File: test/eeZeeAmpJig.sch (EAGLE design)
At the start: 19 parts

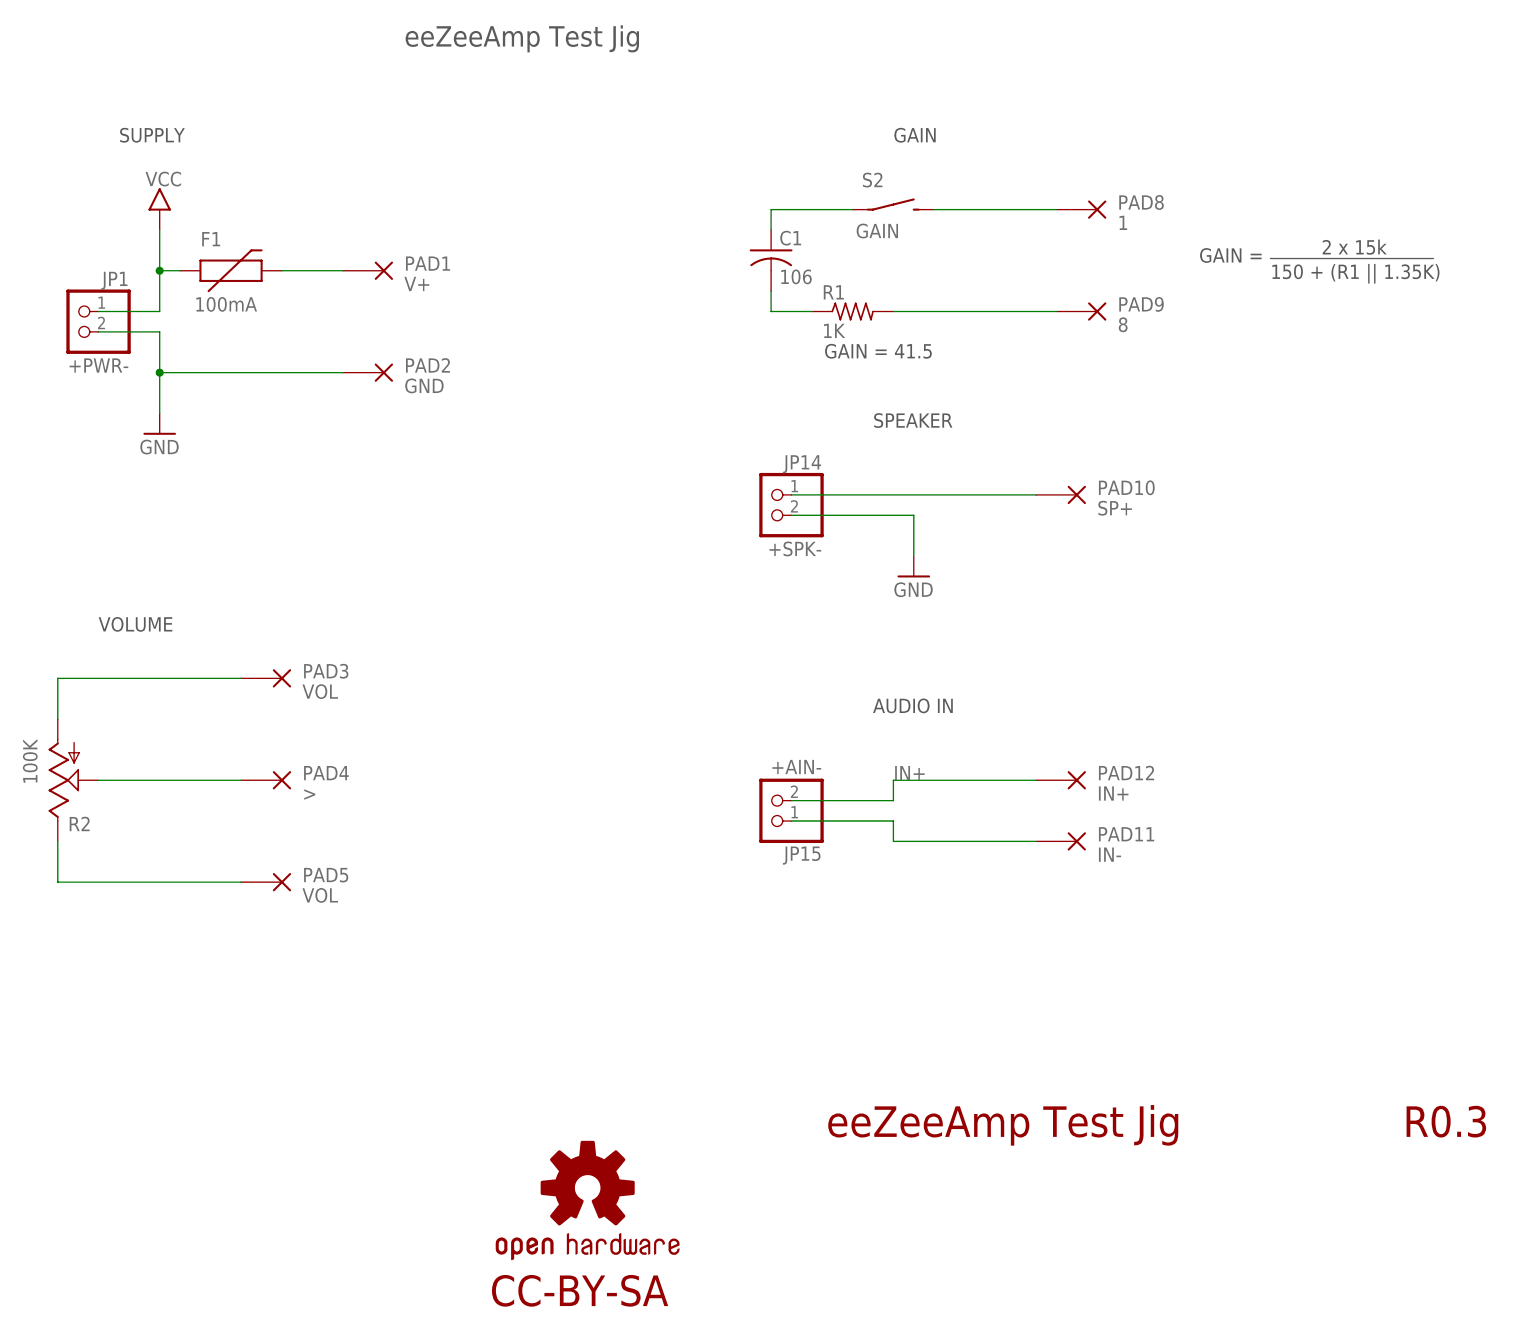
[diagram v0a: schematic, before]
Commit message: added pogo pins for output audio cap
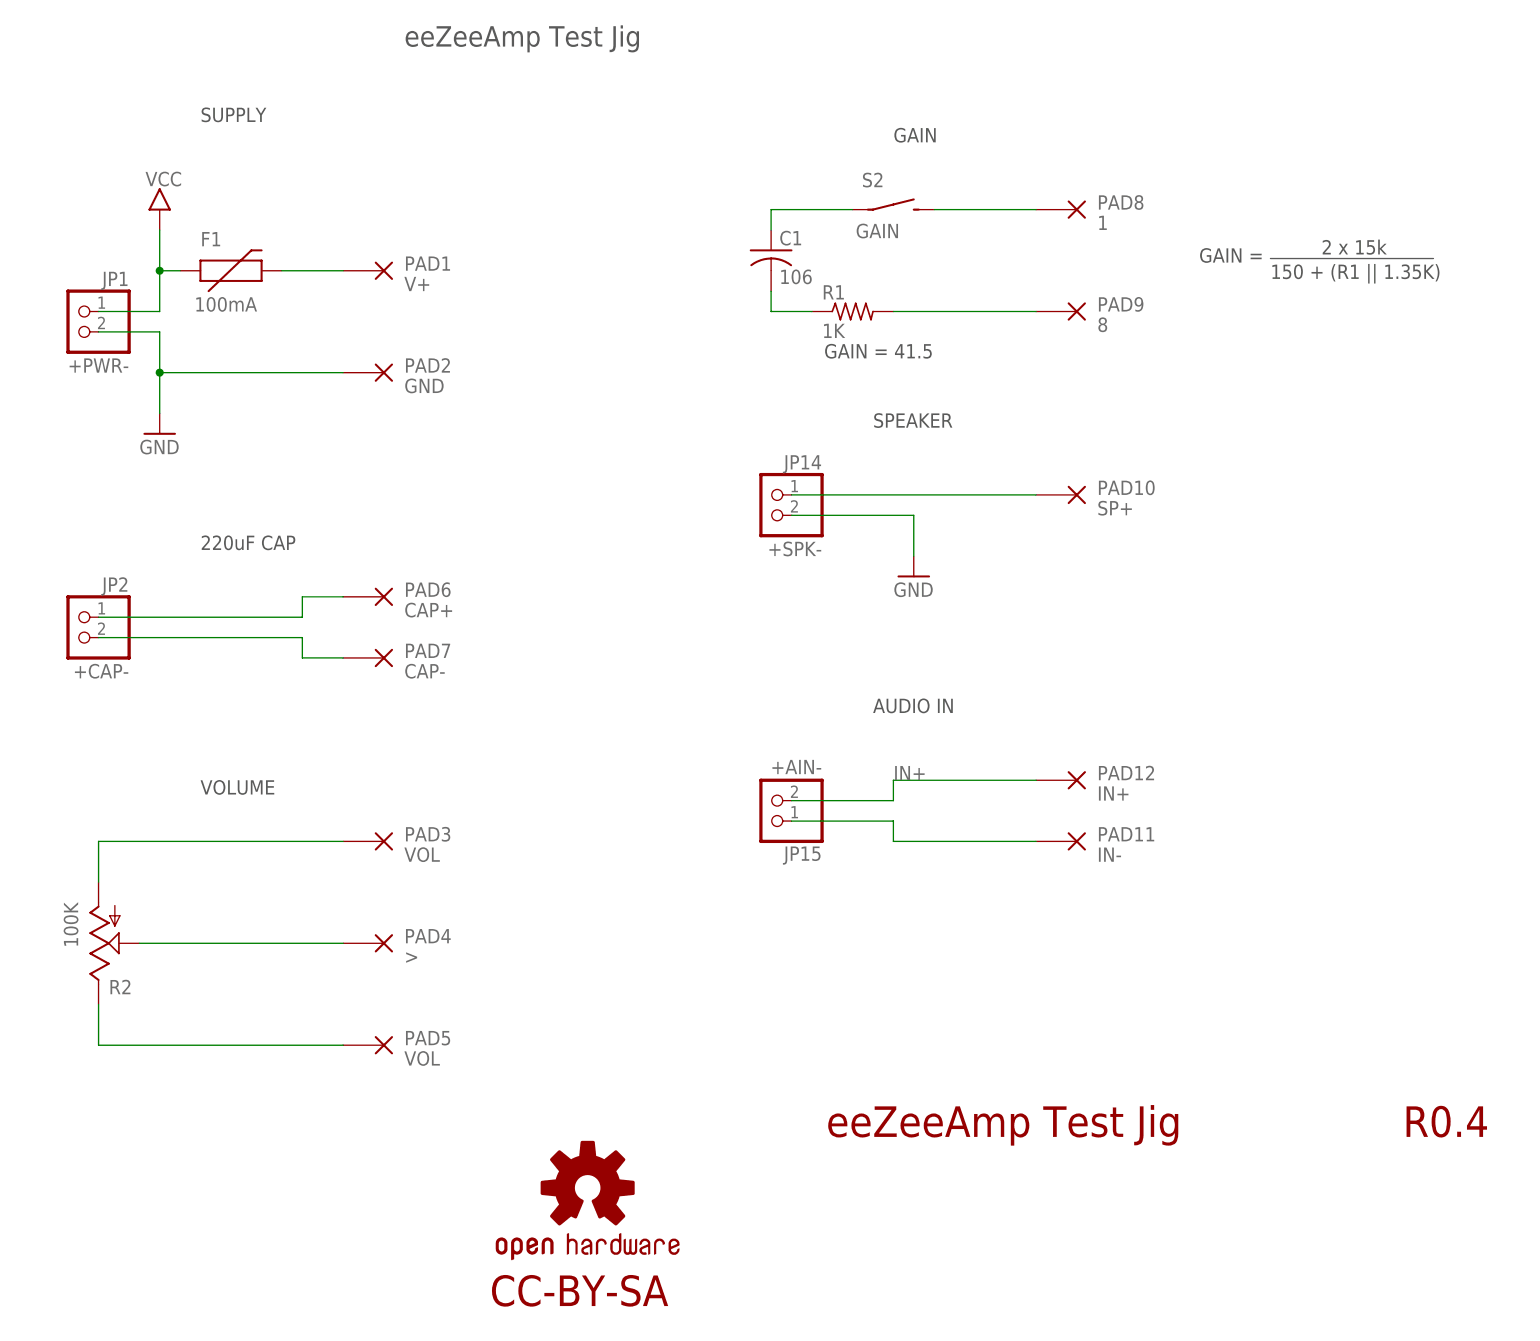
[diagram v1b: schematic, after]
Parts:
- added JP2: +CAP-, pinhead-2:PINHD-1X02_2.54-S
- added PAD6: CAP+, bt_electromech:WIREPAD_1.2MM
- added PAD7: CAP-, bt_electromech:WIREPAD_1.2MM
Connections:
- new net N$2: JP2.1, PAD6.P
- new net N$6: JP2.2, PAD7.P
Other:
- note added: "220uF CAP"
- note added: "R0.4"
- note removed: "R0.3"
- moved on the sheet: PAD3, PAD4, PAD5, PAD8, PAD9, R2
